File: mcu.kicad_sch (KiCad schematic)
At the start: 29 parts

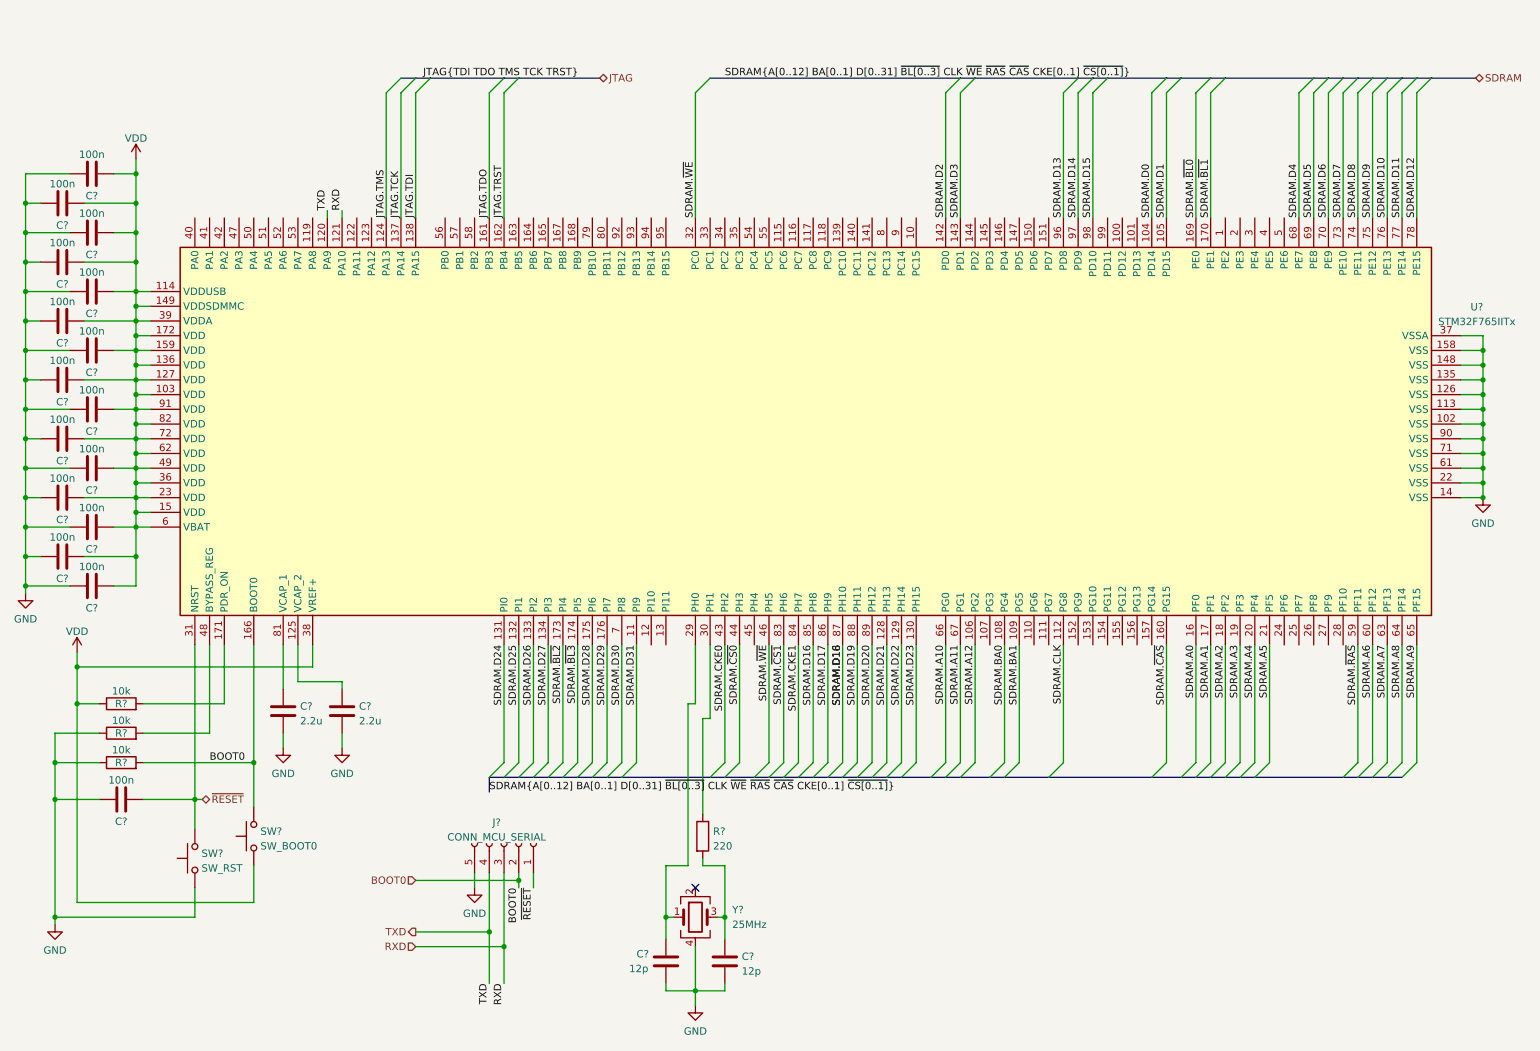
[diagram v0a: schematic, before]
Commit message: Complete wiring of SDRAM.
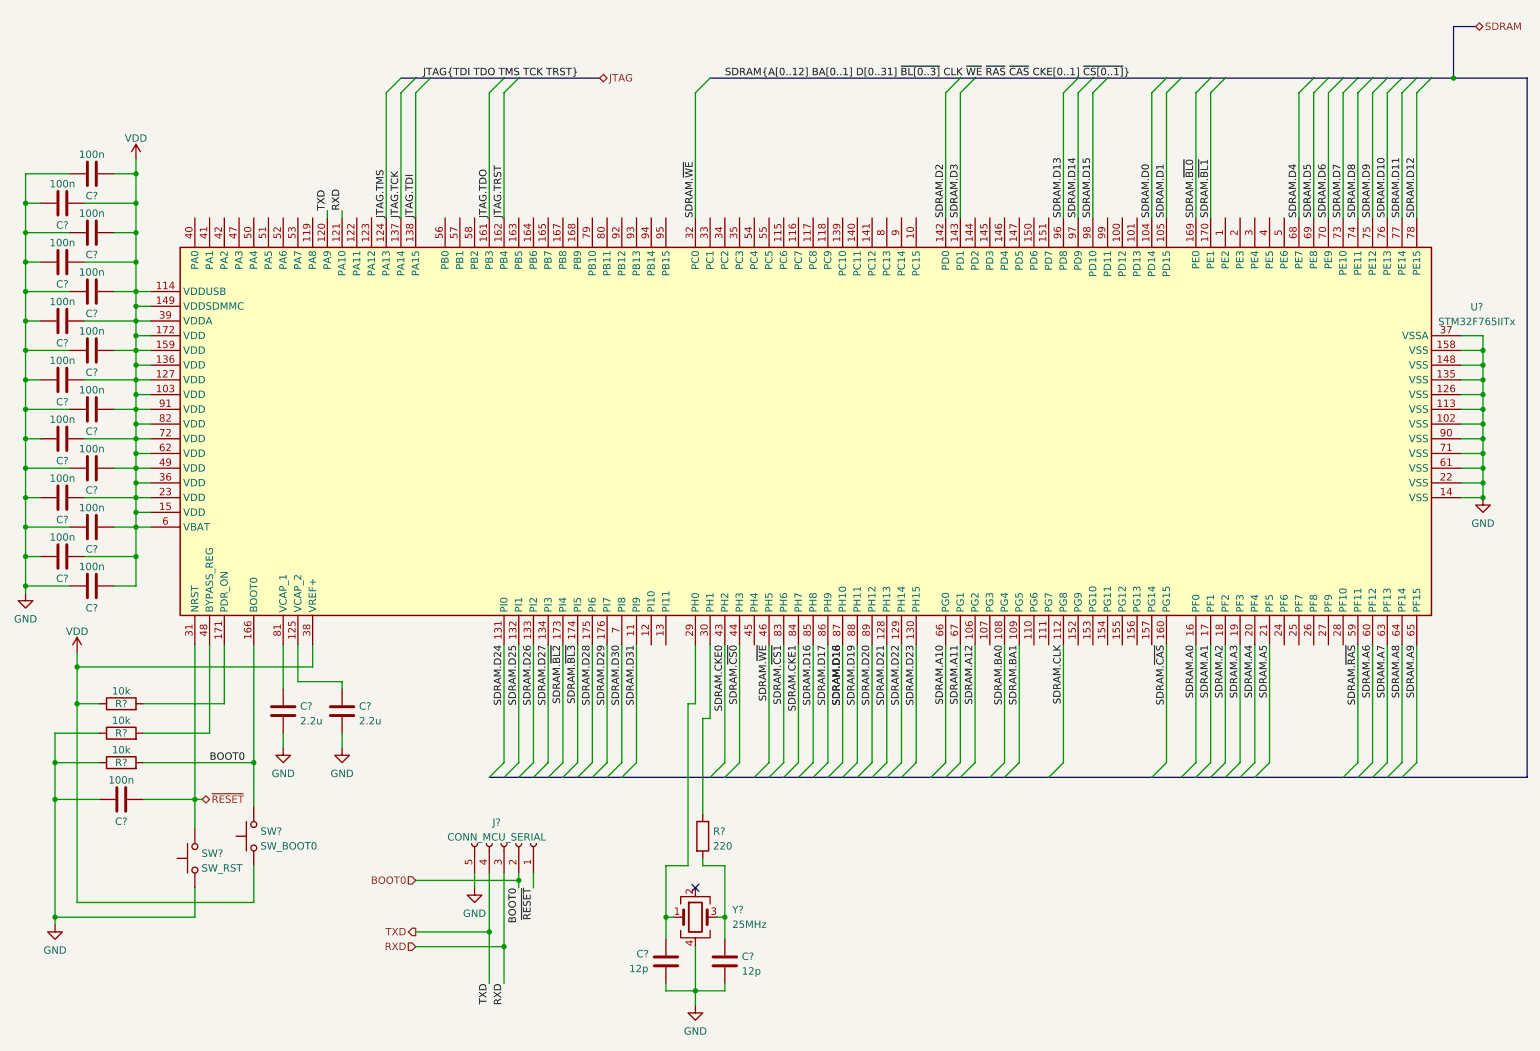
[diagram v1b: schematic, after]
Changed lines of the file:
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@@
   (junction (at 274.32 91.44) (diameter 0) (color 0 0 0 0)
+  )
+  (junction (at 269.24 26.67) (diameter 0) (color 0 0 0 0)
   )
   (junction (at 22.86 58.42) (diameter 0) (color 0 0 0 0)
@@
     (stroke (width 0) (type default) (color 0 0 0 0))
   )
+  (bus (pts (xy 269.24 17.78) (xy 273.05 17.78))
+    (stroke (width 0) (type default) (color 0 0 0 0))
+  )
   (wire (pts (xy 43.18 139.7) (xy 54.61 139.7))
     (stroke (width 0) (type default) (color 0 0 0 0))
@@
     (stroke (width 0) (type default) (color 0 0 0 0))
   )
-  (bus (pts (xy 265.43 26.67) (xy 273.05 26.67))
+  (bus (pts (xy 265.43 26.67) (xy 269.24 26.67))
     (stroke (width 0) (type default) (color 0 0 0 0))
   )
@@
     (stroke (width 0) (type default) (color 0 0 0 0))
   )
+  (bus (pts (xy 269.24 26.67) (xy 269.24 17.78))
+    (stroke (width 0) (type default) (color 0 0 0 0))
+  )
   (wire (pts (xy 260.35 29.21) (xy 260.35 50.8))
     (stroke (width 0) (type default) (color 0 0 0 0))
@@
     (stroke (width 0) (type default) (color 0 0 0 0))
   )
+  (bus (pts (xy 281.94 147.32) (xy 260.35 147.32))
+    (stroke (width 0) (type default) (color 0 0 0 0))
+  )
   (wire (pts (xy 69.85 130.81) (xy 77.47 130.81))
     (stroke (width 0) (type default) (color 0 0 0 0))
@@
     (stroke (width 0) (type default) (color 0 0 0 0))
   )
-  (bus (pts (xy 102.87 147.32) (xy 102.87 149.86))
-    (stroke (width 0) (type default) (color 0 0 0 0))
-  )
   (wire (pts (xy 41.91 83.82) (xy 41.91 86.36))
     (stroke (width 0) (type default) (color 0 0 0 0))
@@
     (stroke (width 0) (type default) (color 0 0 0 0))
   )
+  (bus (pts (xy 269.24 26.67) (xy 281.94 26.67))
+    (stroke (width 0) (type default) (color 0 0 0 0))
+  )
   (wire (pts (xy 54.61 139.7) (xy 54.61 124.46))
     (stroke (width 0) (type default) (color 0 0 0 0))
@@
     (stroke (width 0) (type default) (color 0 0 0 0))
   )
+  (bus (pts (xy 281.94 26.67) (xy 281.94 147.32))
+    (stroke (width 0) (type default) (color 0 0 0 0))
+  )
   (bus (pts (xy 207.01 26.67) (xy 209.55 26.67))
     (stroke (width 0) (type default) (color 0 0 0 0))
@@
   (label "SDRAM.D31" (at 128.27 124.46 270)
     (effects (font (size 1.27 1.27)) (justify right bottom))
-  )
-  (label "SDRAM{A[0..12] BA[0..1] D[0..31] ~{BL[0..3]} CLK ~{WE} ~{RAS} ~{CAS} CKE[0..1] ~{CS[0..1]}}"
-    (at 102.87 149.86 0)
-    (effects (font (size 1.27 1.27)) (justify left bottom))
   )
   (label "SDRAM.CKE0" (at 143.51 124.46 270)
@@
     (effects (font (size 1.27 1.27)) (justify left))
   )
-  (hierarchical_label "SDRAM" (shape bidirectional) (at 273.05 26.67 0)
+  (hierarchical_label "SDRAM" (shape bidirectional) (at 273.05 17.78 0)
     (effects (font (size 1.27 1.27)) (justify left))
   )

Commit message: Add SD card connector.
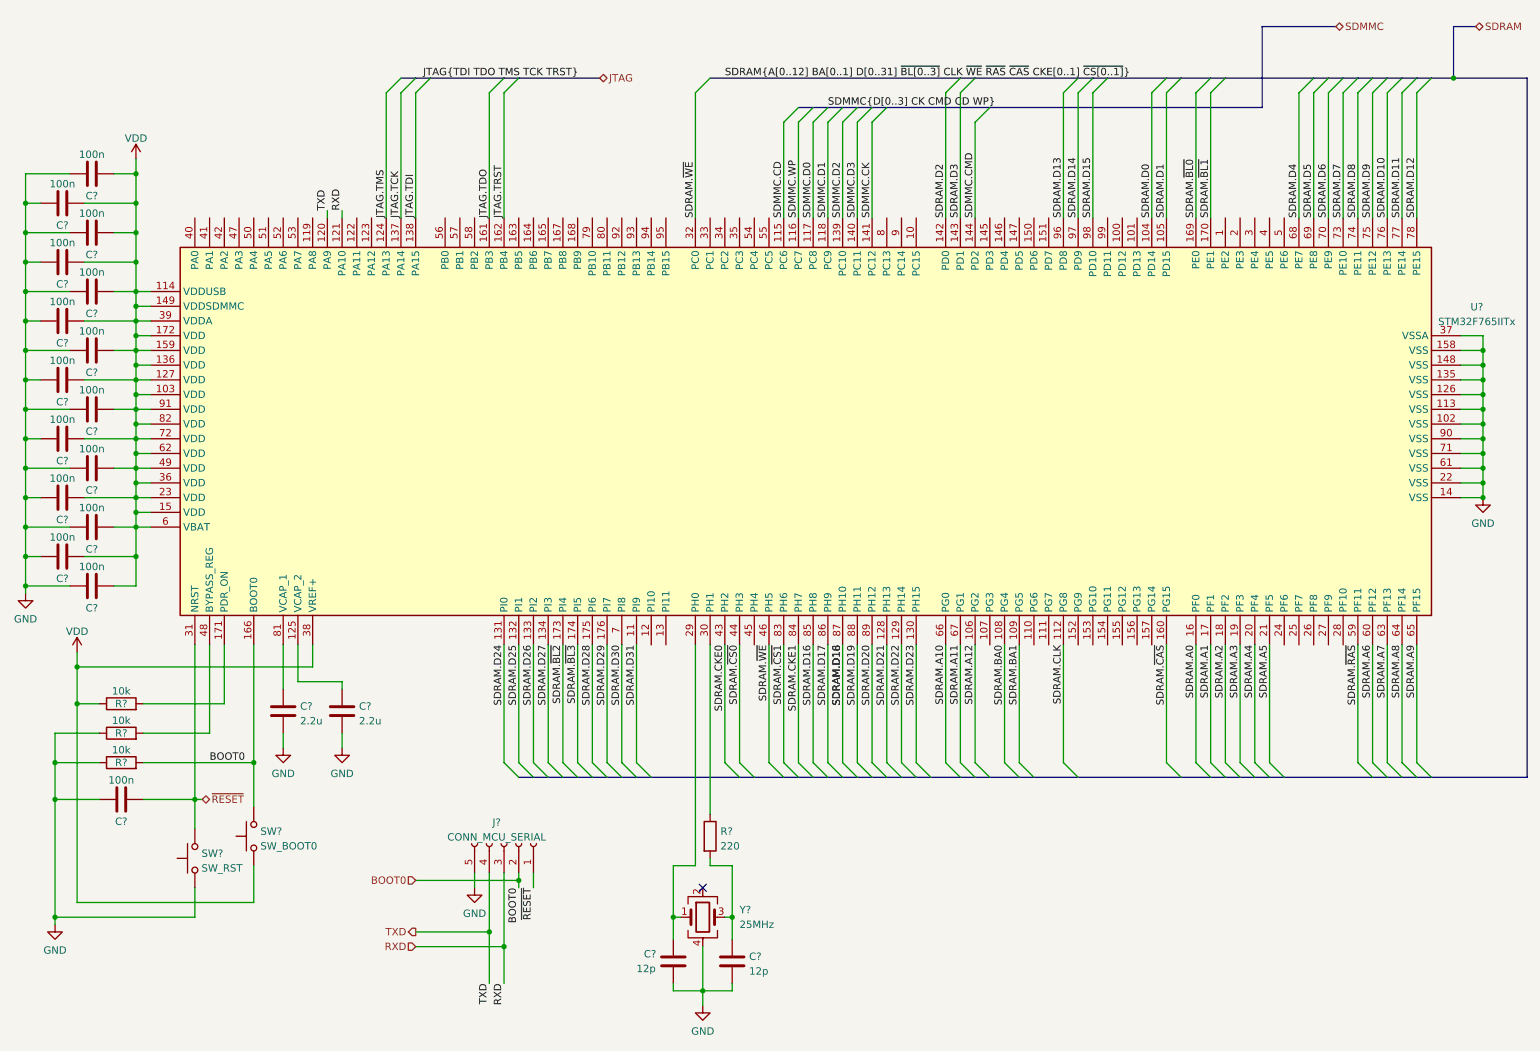
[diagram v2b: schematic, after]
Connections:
- net SDMMC.CD: now reaches U?.115 (PC6)
- net SDMMC.WP: now reaches U?.116 (PC7)
- net SDMMC.D0: now reaches U?.117 (PC8)
- net SDMMC.D1: now reaches U?.118 (PC9)
- net SDMMC.D2: now reaches U?.139 (PC10)
- net SDMMC.D3: now reaches U?.140 (PC11)
- net SDMMC.CK: now reaches U?.141 (PC12)
- net SDMMC.CMD: now reaches U?.144 (PD2)
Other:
- moved on the sheet: C?, R?, Y?

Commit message: Add power supply.
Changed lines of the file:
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@@
   )
   (symbol (lib_id "MCU_ST_STM32F7:STM32F765IITx") (at 156.21 86.36 90) (unit 1)
-    (in_bom yes) (on_board yes) (fields_autoplaced)
-    (property "Reference" "U?" (id 0) (at 273.2564 66.1628 90))
-    (property "Value" "STM32F765IITx" (id 1) (at 273.2564 68.6997 90))
+    (in_bom yes) (on_board yes)
+    (property "Reference" "U?" (id 0) (at 156.21 85.09 90))
+    (property "Value" "STM32F765IITx" (id 1) (at 156.21 87.6269 90))
     (property "Footprint" "Package_QFP:LQFP-176_24x24mm_P0.5mm" (id 2) (at 265.43 119.38 0)
       (effects (font (size 1.27 1.27)) (justify right) hide)
